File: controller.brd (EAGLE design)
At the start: 100 x 80 mm, 46 parts, among them IC1 7805DT, Q3 MOSFET-NCHANNELFDD8780, Q5 MMBT4403, SW1 ROTARTY_ENCODER, U1 ATMEGA328P, Y1 16MHz

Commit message: controller board layout complete.
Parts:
- removed D6: WHITE, SparkFun-LED:LED-1206
- removed S1: (no value), SparkFun-Electromechanical:R_SW_TH
- added Q2: MOSFET-NCHANNELBSS123LT1G, SparkFun-DiscreteSemi:SOT23
- added U$13: SWITCH-SPDT, jt_parts:SWITCH-SPDT-T511006
- D1, D2, D3, D4, D5: device SparkFun-LED:LED-1206 -> SparkFun-LED:LED3MM
- SW1: value ROTARTY_ENCODER -> ROT_ENCODER; device SparkFun-Electromechanical:ROTARY_ENC_PLAIN -> jt_parts:ROT-ENCODER-EVEGA
- moved S4 53.0 mm to (63.5, 57.1), turned to 180 degrees
- moved U$14 42.0 mm to (63.5, 52.7)
- moved D1 8.89 mm to (8.89, 21.6)
- moved D2 8.89 mm to (8.89, 26.7)
- moved D3 8.89 mm to (8.89, 31.8)
- moved D4 8.89 mm to (8.89, 36.8)
- moved D5 8.89 mm to (8.89, 41.9)
- moved C8 5.08 mm to (21.6, 16.5)
- moved C9 5.08 mm to (21.6, 26.7)
- moved S6 5.08 mm to (15.9, 17.8)
- moved U$2 5.08 mm to (22.9, 30.5)
- moved U1 5.08 mm to (37.5, 26.7)
- moved C6 5.08 mm to (15.2, 22.9)
- moved C7 5.08 mm to (38.1, 34.3)
- moved U$10 5.08 mm to (15.2, 31.1)
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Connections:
- removed net N$8: 12V_IN.2, S1.P$2
- removed net NIGHT: U$3.1
- new net N$12: D1.K, D2.K, D3.K, D4.K, D5.K, Q2.3
- new net NITE: Q2.1, U1.23
- net 12V: now also 12V_IN.2, U$13.P$3, U$13.P$4, U$13.P$5; no longer S1.P$1, S1.P$3
- net 5V: now also JP1.6, JP2.4, U$12.2, U$3.1
- net ENC_A: now also SW1.P$1; no longer SW1.A
- net ENC_B: now also SW1.P$2; no longer SW1.B
- net GND: now also Q2.2, SW1.P$3; no longer D1.C, D2.C, D3.C, D4.C, D5.C, D6.C
- net N$9: no longer D6.A
- net VCC: no longer JP1.6, JP2.4, U$12.2
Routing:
- net 5V: track 43.8 -> 210.8 mm, vias 0 -> 2
- net 12V: track 0.00 -> 79.1 mm
- net VBATT: track 0.00 -> 69.9 mm, vias 0 -> 2
- net SW2: track 0.00 -> 49.4 mm, vias 0 -> 2
- net PWM: track 0.00 -> 47.3 mm, vias 0 -> 4
- net SW1: track 0.00 -> 42.1 mm, vias 0 -> 2
- net N$12: track 0.00 -> 35.0 mm, vias 0 -> 1
- net ENC_B: track 12.6 -> 44.0 mm
- net ENC_A: track 16.1 -> 42.8 mm
- net N$9: track 0.00 -> 24.7 mm
- net NITE: track 0.00 -> 22.3 mm, vias 0 -> 2
- net SCK: track 18.3 -> 27.0 mm, vias 1 -> 2
- net SERIAL: track 13.7 -> 22.3 mm, vias 1 -> 2
- net RCK: track 15.6 -> 24.0 mm, vias 1 -> 2
- net GND: track 54.3 -> 62.5 mm, vias 6 -> 13
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- removed copper zone on layer 1, net 12V

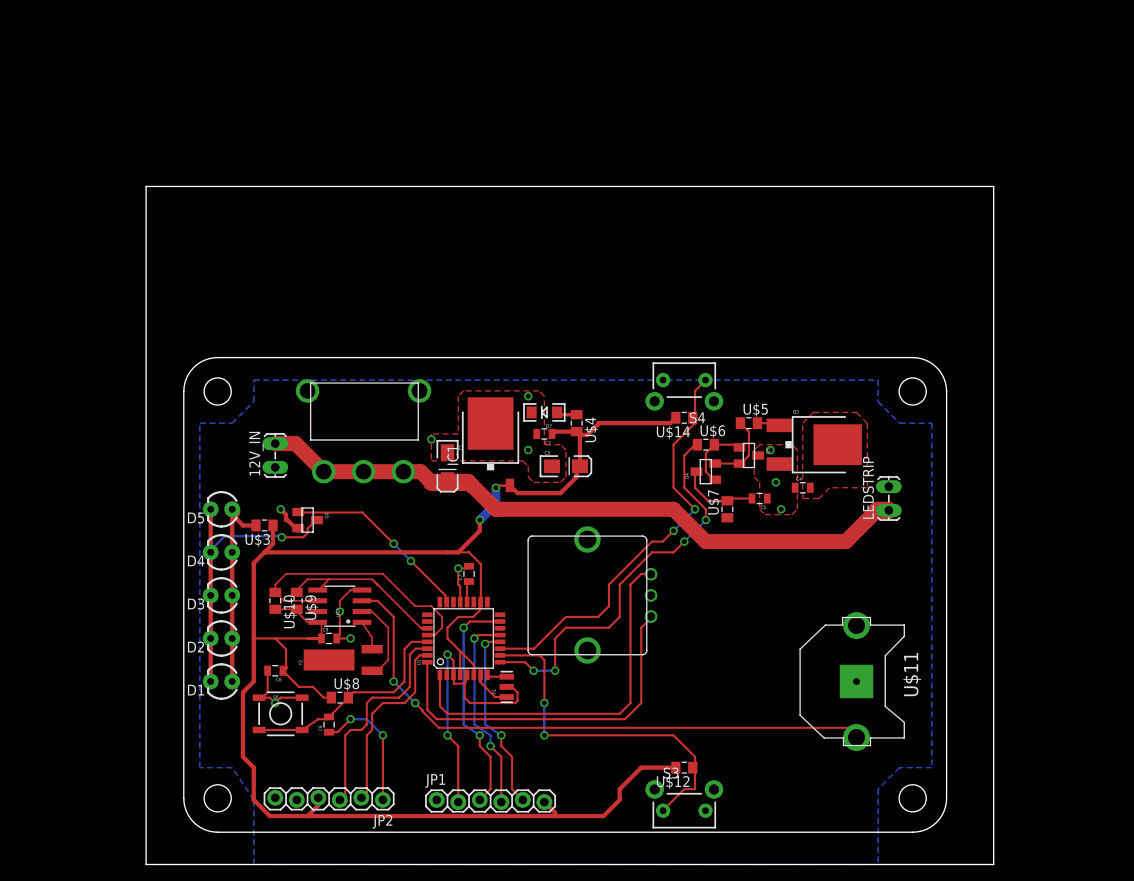
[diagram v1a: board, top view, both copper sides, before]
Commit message: added fuse. tore up power traces.
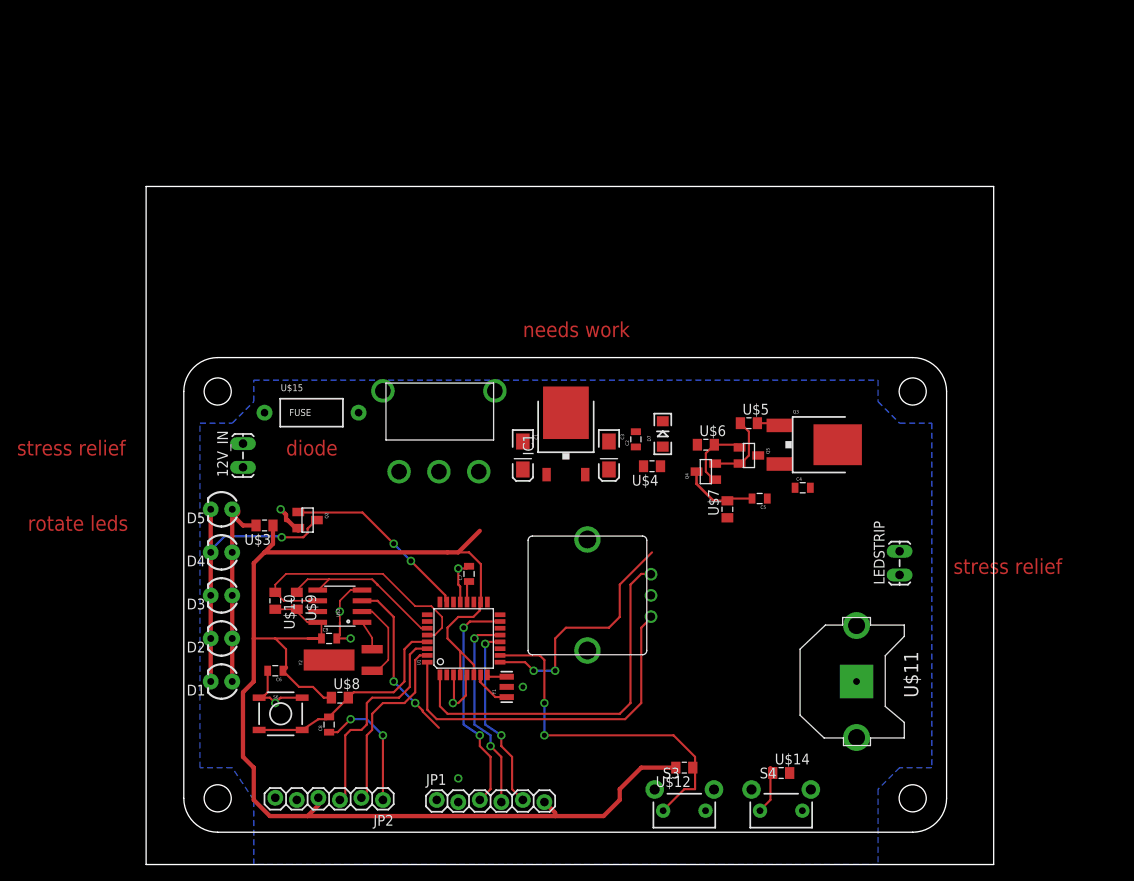
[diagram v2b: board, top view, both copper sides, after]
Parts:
- added U$15: FUSE, jt_parts:FUSE-LITTLE-251
- moved S4 52.1 mm to (74.9, 6.35), turned to 0 degrees
- moved U$14 43.4 mm to (74.9, 10.8), turned to 0 degrees
- moved D7 14.2 mm to (61.0, 50.8), turned to 90 degrees
- moved C2 10.8 mm to (57.8, 50.2), turned to 90 degrees
- moved U$4 10.2 mm to (59.7, 47.0), turned to 180 degrees
- moved C1 8.98 mm to (44.5, 48.3)
- moved IC1 8.98 mm to (49.5, 50.8)
- moved U$13 8.89 mm to (27.9, 55.9)
- moved LEDSTRIP 7.73 mm to (88.9, 34.3)
- moved C3 5.24 mm to (54.6, 48.3), turned to 270 degrees
- moved 12V_IN 3.81 mm to (11.4, 47.0)
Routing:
- net 12V: track 79.1 -> 0.00 mm
- net VBATT: track 69.9 -> 21.2 mm
- net SW2: track 49.4 -> 5.81 mm, vias 2 -> 0
- net 5V: track 210.8 -> 173.0 mm, vias 2 -> 0
- net GND: track 62.5 -> 36.1 mm, vias 13 -> 8
- net PWM: track 47.3 -> 28.6 mm, vias 4 -> 2
- net N$10: track 2.42 -> 0.38 mm
- net N$2: track 9.45 -> 8.93 mm
- removed copper zone on layer 1, net 12V-RETURN
- removed copper zone on layer 1, net GND
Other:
- board text added: "diode"
- board text added: "needs work"
- board text added: "rotate leds"
- board text added: "stress relief"

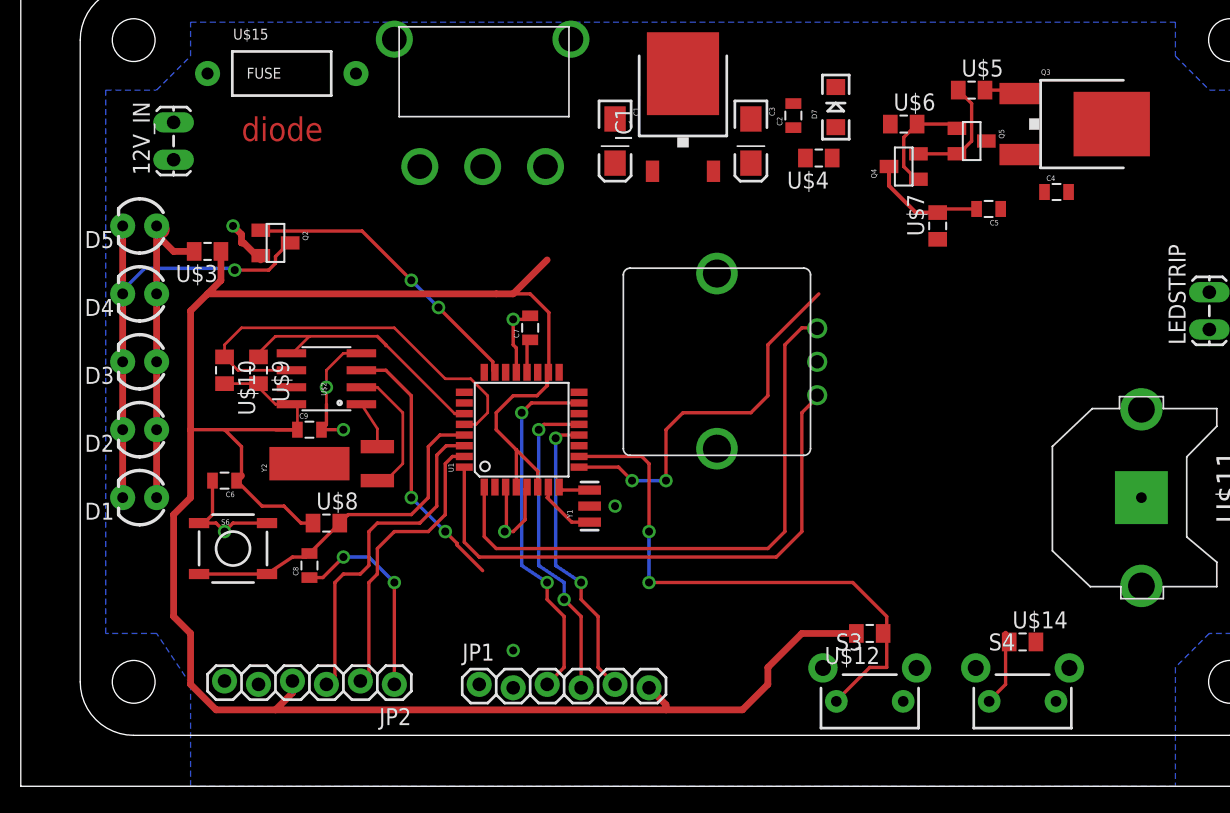
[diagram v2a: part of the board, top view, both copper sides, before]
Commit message: commit prior to adding reverse polarity protection.
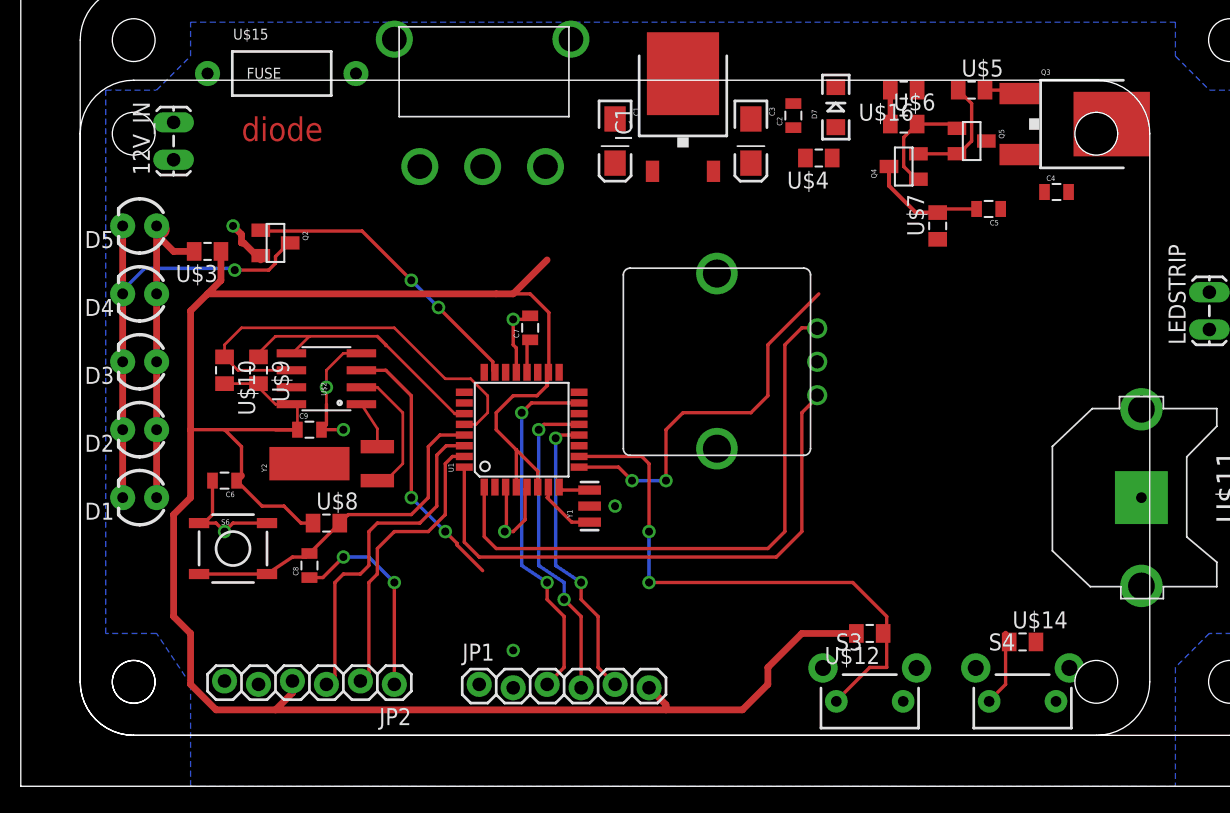
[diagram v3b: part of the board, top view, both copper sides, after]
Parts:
- added U$16: (no value), jt_parts:RESISTOR-0805
- added U$17: (no value), dp_pcb:DP8049_V1
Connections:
- net GND: now also U$16.1
- net PWM: now also U$16.2
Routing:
- net PWM: track 28.6 -> 31.1 mm
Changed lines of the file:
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@@
 <element name="U$13" library="jt_parts" package="SWITCH-SPDT-T511006" value="SWITCH-SPDT" x="27.94" y="55.88"/>
 <element name="U$15" library="jt_parts" package="FUSE-LITTLE-251" value="FUSE" x="20.32" y="53.34"/>
+<element name="U$16" library="jt_parts" package="RESISTOR-0805" value="" x="66.04" y="52.07" rot="R180"/>
+<element name="U$17" library="dp_pcb" package="DP8049_V1" value="" x="4.445" y="3.81"/>
 </elements>
 <signals>
@@
 <wire x1="36.83" y1="19.05" x2="36.195" y2="19.05" width="0.254" layer="1"/>
 <via x="44.45" y="20.955" extent="1-16" drill="0.6"/>
+<contactref element="U$16" pad="1"/>
 <wire x1="72.22" y1="48.26" x2="74.7" y2="47.25" width="0" layer="19" extent="1-1"/>
 <wire x1="76.57" y1="44.45" x2="74.7" y2="47.25" width="0" layer="19" extent="1-1"/>
 <wire x1="73.29" y1="43.18" x2="76.57" y2="44.45" width="0" layer="19" extent="1-1"/>
-<wire x1="77.43" y1="6.35" x2="72.22" y2="48.26" width="0" layer="19" extent="1-1"/>
-<wire x1="43.18" y1="20.955" x2="44.45" y2="20.955" width="0" layer="19" extent="1-1"/>
-<wire x1="44.45" y1="49.91" x2="38.1" y2="35.19" width="0" layer="19" extent="1-1"/>
-<wire x1="49.53" y1="53.3" x2="44.45" y2="49.91" width="0" layer="19" extent="1-1"/>
-<wire x1="60.96" y1="52.3" x2="49.53" y2="53.3" width="0" layer="19" extent="1-1"/>
+<wire x1="60.96" y1="52.3" x2="72.22" y2="48.26" width="0" layer="19" extent="1-1"/>
 <wire x1="57.785" y1="51.065" x2="60.96" y2="52.3" width="0" layer="19" extent="1-1"/>
 <wire x1="54.61" y1="49.91" x2="57.785" y2="51.065" width="0" layer="19" extent="1-1"/>
+<wire x1="49.53" y1="53.3" x2="54.61" y2="49.91" width="0" layer="19" extent="1-1"/>
+<wire x1="44.45" y1="49.91" x2="49.53" y2="53.3" width="0" layer="19" extent="1-1"/>
+<wire x1="38.1" y1="35.19" x2="44.45" y2="49.91" width="0" layer="19" extent="1-1"/>
+<wire x1="37.865" y1="22.3774" x2="37.065" y2="30.9626" width="0" layer="19" extent="1-1"/>
+<wire x1="42.545" y1="20.955" x2="37.865" y2="22.3774" width="0" layer="19" extent="1-1"/>
+<wire x1="44.45" y1="20.955" x2="43.18" y2="20.955" width="0" layer="19" extent="1-1"/>
+<wire x1="36.83" y1="10.16" x2="36.83" y2="19.05" width="0" layer="19" extent="1-1"/>
+<wire x1="36.83" y1="7.366" x2="36.83" y2="10.16" width="0" layer="19" extent="1-1"/>
+<wire x1="25.4762" y1="32.385" x2="36.83" y2="33.02" width="0" layer="19" extent="1-1"/>
+<wire x1="22.86" y1="26.67" x2="22.86" y2="27.04" width="0" layer="19" extent="1-1"/>
+<wire x1="18.415" y1="19.685" x2="22.49" y2="26.67" width="0" layer="19" extent="1-1"/>
+<wire x1="17.95" y1="39.37" x2="24.13" y2="32.385" width="0" layer="19" extent="1-1"/>
+<wire x1="11.43" y1="46.863" x2="15.875" y2="41.91" width="0" layer="19" extent="1-1"/>
+<wire x1="15.24" y1="7.874" x2="15.24" y2="19.05" width="0" layer="19" extent="1-1"/>
+<wire x1="17.78" y1="7.62" x2="15.24" y2="7.874" width="0" layer="19" extent="1-1"/>
+<wire x1="59.57" y1="31.75" x2="73.29" y2="43.18" width="0" layer="19" extent="1-1"/>
+<wire x1="83.82" y1="21.59" x2="76.57" y2="44.45" width="0" layer="19" extent="1-1"/>
+<wire x1="77.43" y1="6.35" x2="83.82" y2="21.59" width="0" layer="19" extent="1-1"/>
+<wire x1="66" y1="6.35" x2="77.43" y2="6.35" width="0" layer="19" extent="1-1"/>
+<wire x1="67.04" y1="52.07" x2="15.24" y2="7.874" width="0" layer="19" extent="1-1"/>
 </signal>
 <signal name="RCK">
@@
 <wire x1="55.88" y1="29.21" x2="55.88" y2="33.02" width="0.254" layer="1"/>
 <wire x1="55.88" y1="33.02" x2="59.69" y2="36.83" width="0.254" layer="1"/>
+<contactref element="U$16" pad="2"/>
+<wire x1="65.04" y1="52.07" x2="65.04" y2="49.53" width="0.4064" layer="1"/>
 <wire x1="59.69" y1="36.83" x2="65.04" y2="49.53" width="0" layer="19" extent="1-1"/>
 </signal>

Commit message: removed smaller board reference outline.
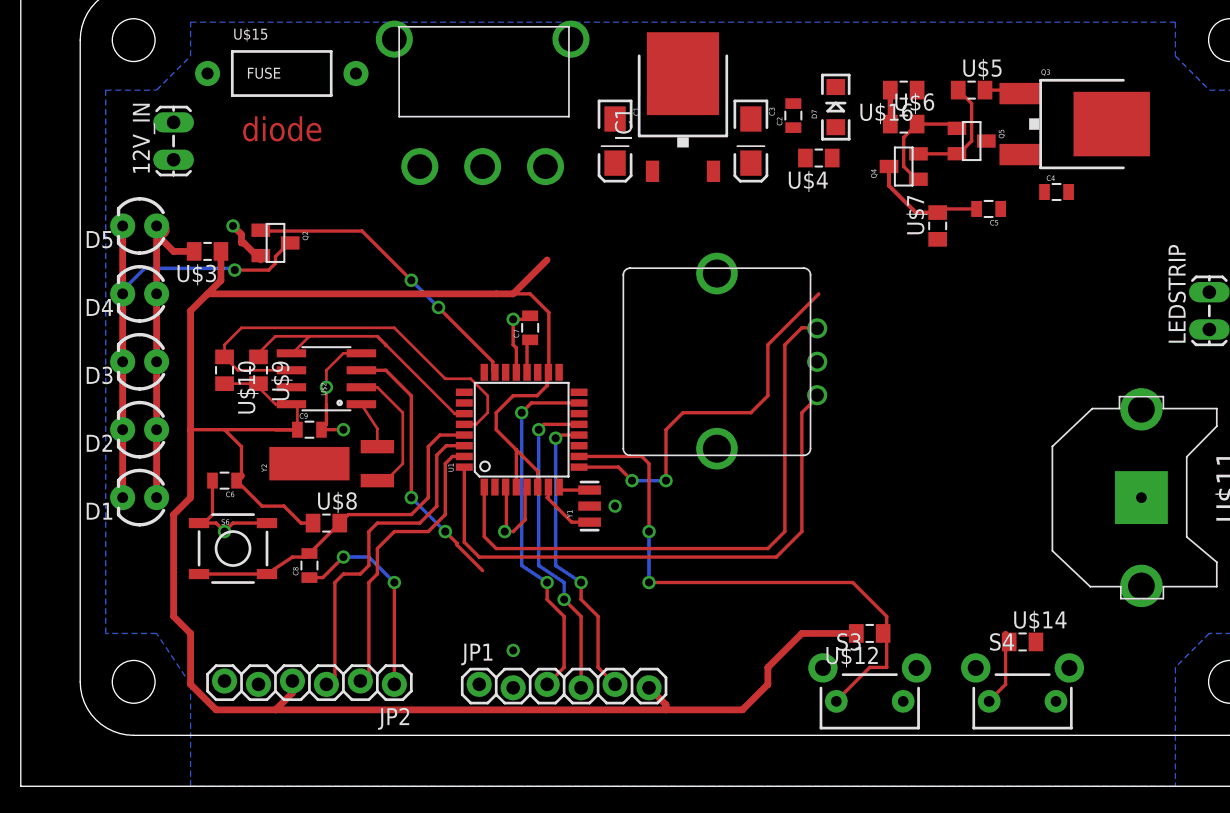
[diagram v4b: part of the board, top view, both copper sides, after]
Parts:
- removed U$17: (no value), dp_pcb:DP8049_V1
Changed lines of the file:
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@@
 <element name="U$15" library="jt_parts" package="FUSE-LITTLE-251" value="FUSE" x="20.32" y="53.34"/>
 <element name="U$16" library="jt_parts" package="RESISTOR-0805" value="" x="66.04" y="52.07" rot="R180"/>
-<element name="U$17" library="dp_pcb" package="DP8049_V1" value="" x="4.445" y="3.81"/>
 </elements>
 <signals>
